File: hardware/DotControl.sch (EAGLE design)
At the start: 26 parts, among them CN1 1X4-BIG, J3 USB-MICROB, SW2 Previous, SW5 Previous, SW6 Next, SW8 Ok, U1 ATMEGA328P-MU-QFN32, U2 TMP102

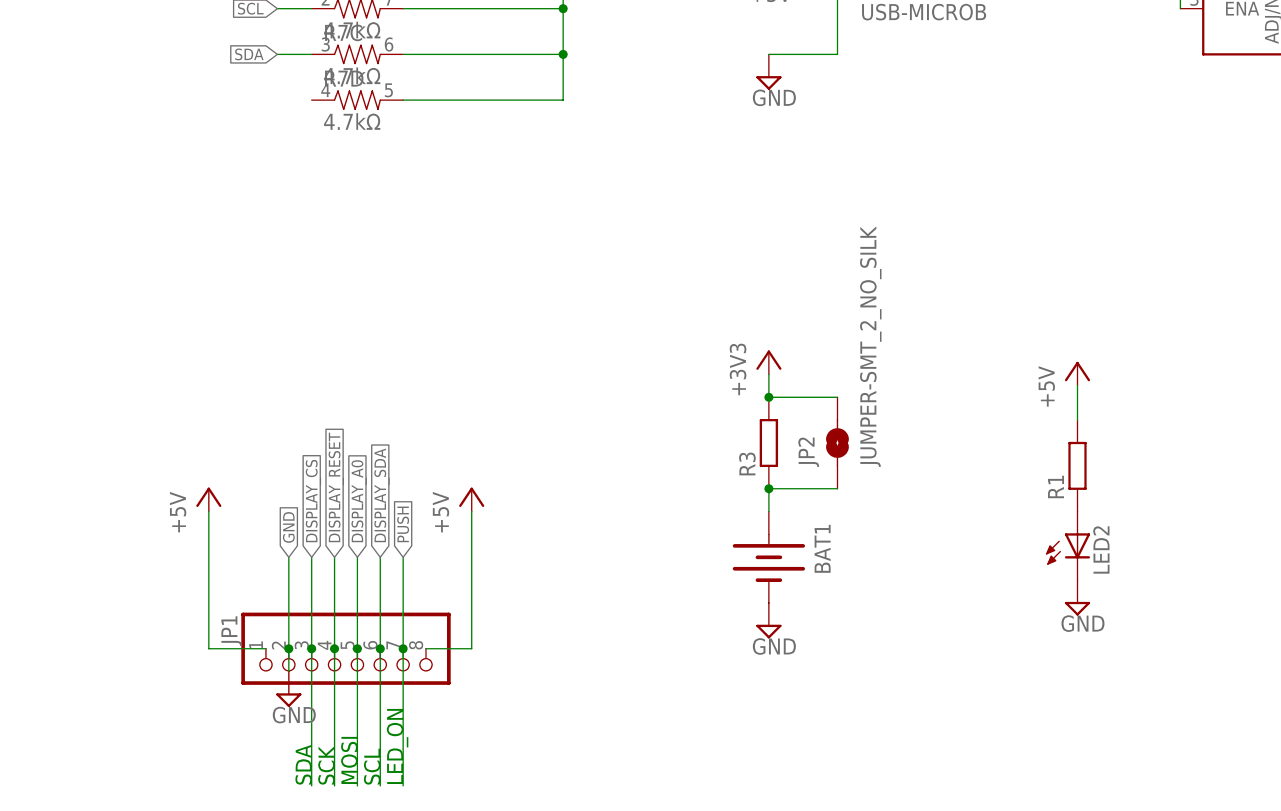
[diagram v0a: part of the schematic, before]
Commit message: Update display supply to 3.3V, charging of battery
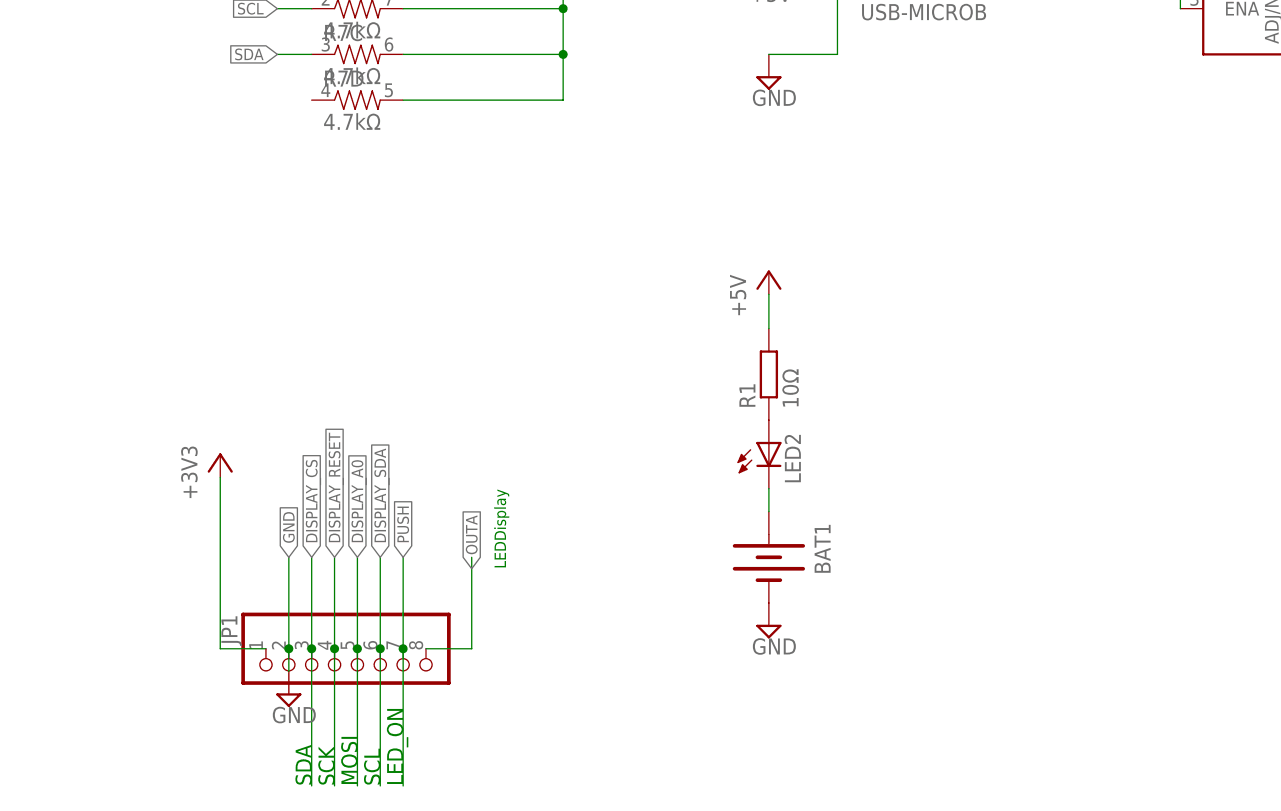
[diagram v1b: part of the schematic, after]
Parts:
- removed JP2: JUMPER-SMT_2_NO_SILK, SparkFun-Jumpers:JUMPER-SMT_2_NO_SILK
- removed R3: (no value), resistor:R-EU_R0603
- R1: value (none) -> 10Ω
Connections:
- removed net N$16: BAT1.+, JP2.1, R3.1
- new net N$3: BAT1.+, LED2.C
- net +3V3: now also JP1.1; no longer JP2.2, R3.2
- net +5V: no longer JP1.1, JP1.8
- net GND: no longer LED2.C
- net OUTA: now also JP1.8
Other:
- note added: "LEDDisplay"
- moved on the sheet: LED2, R1
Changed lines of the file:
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@@
 <setting verticaltext="up"/>
 </settings>
-<grid distance="0.1" unitdist="inch" unit="inch" style="lines" multiple="1" display="no" altdistance="0.01" altunitdist="inch" altunit="inch"/>
+<grid distance="0.05" unitdist="inch" unit="inch" style="lines" multiple="1" display="no" altdistance="0.01" altunitdist="inch" altunit="inch"/>
 <layers>
 <layer number="1" name="Top" color="4" fill="1" visible="no" active="no"/>
@@
 <part name="JP1" library="adafruit" deviceset="PINHD-1X8" device="CLEANBIG"/>
 <part name="SUPPLY8" library="supply2" deviceset="GND" device=""/>
-<part name="+3V3" library="supply1" deviceset="+3V3" device=""/>
 <part name="BAT1" library="Battery" deviceset="BATTERY" device="20PTH"/>
 <part name="+3V14" library="supply1" deviceset="+3V3" device=""/>
@@
 <part name="SUPPLY18" library="supply2" deviceset="GND" device=""/>
 <part name="CN1" library="adafruit" deviceset="1X4" device="-BIG"/>
-<part name="R3" library="resistor" deviceset="R-EU_" device="R0603"/>
-<part name="JP2" library="SparkFun-Jumpers" deviceset="JUMPER-SMT_2_NO" device="_SILK"/>
 <part name="SJ1" library="SparkFun" deviceset="SOLDERJUMPER" device="TRACE"/>
 <part name="+3V7" library="supply1" deviceset="+3V3" device=""/>
-<part name="R1" library="resistor" deviceset="R-EU_" device="R0603"/>
+<part name="R1" library="resistor" deviceset="R-EU_" device="R0603" value="10Ω"/>
 <part name="LED2" library="SparkFun" deviceset="LED" device="0603"/>
-<part name="SUPPLY5" library="supply2" deviceset="GND" device=""/>
-<part name="P+1" library="supply1" deviceset="+5V" device=""/>
-<part name="P+2" library="supply1" deviceset="+5V" device=""/>
 <part name="P+5" library="supply1" deviceset="+5V" device=""/>
 <part name="U2" library="SparkFun" deviceset="TMP102" device=""/>
@@
 <part name="SUPPLY12" library="supply2" deviceset="GND" device=""/>
 <part name="SUPPLY7" library="supply2" deviceset="GND" device=""/>
+<part name="+3V3" library="supply1" deviceset="+3V3" device=""/>
 </parts>
 <sheets>
@@
 <text x="71.12" y="114.3" size="1.778" layer="91" rot="R90">SCL</text>
 <text x="73.66" y="114.3" size="1.778" layer="91" rot="R90">LED_ON</text>
+<text x="85.09" y="138.43" size="1.27" layer="91" rot="R90">LEDDisplay</text>
 </plain>
 <instances>
@@
 <instance part="JP1" gate="G$1" x="66.04" y="127" rot="MR270"/>
 <instance part="SUPPLY8" gate="GND" x="114.3" y="132.08"/>
-<instance part="+3V3" gate="G$1" x="114.3" y="162.56"/>
 <instance part="BAT1" gate="G$1" x="114.3" y="139.7" rot="R270"/>
 <instance part="+3V14" gate="G$1" x="177.8" y="289.56"/>
@@
 <instance part="SUPPLY18" gate="GND" x="218.44" y="157.48"/>
 <instance part="CN1" gate="G$1" x="231.14" y="165.1"/>
-<instance part="R3" gate="G$1" x="114.3" y="152.4" rot="R90"/>
-<instance part="JP2" gate="G$1" x="121.92" y="152.4" rot="R90"/>
 <instance part="SJ1" gate="1" x="80.01" y="219.71" rot="R90"/>
 <instance part="+3V7" gate="G$1" x="80.01" y="227.33"/>
-<instance part="R1" gate="G$1" x="148.59" y="149.86" rot="R90"/>
-<instance part="LED2" gate="G$1" x="148.59" y="142.24"/>
-<instance part="SUPPLY5" gate="GND" x="148.59" y="134.62"/>
-<instance part="P+1" gate="1" x="81.28" y="147.32"/>
-<instance part="P+2" gate="1" x="52.07" y="147.32"/>
-<instance part="P+5" gate="1" x="148.59" y="161.29"/>
+<instance part="R1" gate="G$1" x="114.3" y="160.02" rot="R90"/>
+<instance part="LED2" gate="G$1" x="114.3" y="152.4"/>
+<instance part="P+5" gate="1" x="114.3" y="171.45"/>
 <instance part="U2" gate="G$1" x="226.06" y="104.14"/>
 <instance part="SUPPLY15" gate="GND" x="213.36" y="96.52"/>
@@
 <instance part="SUPPLY12" gate="GND" x="203.2" y="99.06"/>
 <instance part="SUPPLY7" gate="GND" x="254" y="96.52"/>
+<instance part="+3V3" gate="G$1" x="53.34" y="151.13"/>
 </instances>
 <busses>
@@
 <pinref part="SUPPLY19" gate="GND" pin="GND"/>
 <wire x1="62.23" y1="220.98" x2="62.23" y2="227.33" width="0.1524" layer="91"/>
-</segment>
-<segment>
-<pinref part="LED2" gate="G$1" pin="C"/>
-<pinref part="SUPPLY5" gate="GND" pin="GND"/>
 </segment>
 <segment>
@@
 </segment>
 <segment>
-<pinref part="+3V3" gate="G$1" pin="+3V3"/>
-<pinref part="R3" gate="G$1" pin="2"/>
-<wire x1="114.3" y1="157.48" x2="114.3" y2="160.02" width="0.1524" layer="91"/>
-<wire x1="121.92" y1="157.48" x2="114.3" y2="157.48" width="0.1524" layer="91"/>
-<junction x="114.3" y="157.48"/>
-<pinref part="JP2" gate="G$1" pin="2"/>
-</segment>
-<segment>
 <pinref part="SJ1" gate="1" pin="2"/>
 <pinref part="+3V7" gate="G$1" pin="+3V3"/>
@@
 <junction x="203.2" y="109.22"/>
 <pinref part="U2" gate="G$1" pin="VCC"/>
+</segment>
+<segment>
+<pinref part="+3V3" gate="G$1" pin="+3V3"/>
+<pinref part="JP1" gate="G$1" pin="1"/>
+<wire x1="53.34" y1="148.59" x2="53.34" y2="129.54" width="0.1524" layer="91"/>
+<wire x1="53.34" y1="129.54" x2="58.42" y2="129.54" width="0.1524" layer="91"/>
 </segment>
 </net>
@@
 </segment>
 <segment>
-<pinref part="P+1" gate="1" pin="+5V"/>
-<wire x1="81.28" y1="144.78" x2="81.28" y2="129.54" width="0.1524" layer="91"/>
-<pinref part="JP1" gate="G$1" pin="8"/>
-<wire x1="76.2" y1="129.54" x2="81.28" y2="129.54" width="0.1524" layer="91"/>
-</segment>
-<segment>
-<pinref part="P+2" gate="1" pin="+5V"/>
-<pinref part="JP1" gate="G$1" pin="1"/>
-<wire x1="52.07" y1="144.78" x2="52.07" y2="129.54" width="0.1524" layer="91"/>
-<wire x1="52.07" y1="129.54" x2="58.42" y2="129.54" width="0.1524" layer="91"/>
-</segment>
-<segment>
 <pinref part="R1" gate="G$1" pin="2"/>
-<wire x1="148.59" y1="154.94" x2="148.59" y2="158.75" width="0.1524" layer="91"/>
+<wire x1="114.3" y1="165.1" x2="114.3" y2="168.91" width="0.1524" layer="91"/>
 <pinref part="P+5" gate="1" pin="+5V"/>
 </segment>
@@
 <wire x1="327.66" y1="236.22" x2="330.2" y2="236.22" width="0.1524" layer="91"/>
 <label x="330.2" y="236.22" size="1.27" layer="95" xref="yes"/>
+</segment>
+<segment>
+<pinref part="JP1" gate="G$1" pin="8"/>
+<wire x1="76.2" y1="129.54" x2="81.28" y2="129.54" width="0.1524" layer="91"/>
+<wire x1="81.28" y1="129.54" x2="81.28" y2="139.7" width="0.1524" layer="91"/>
+<label x="81.28" y="138.43" size="1.27" layer="95" rot="R90" xref="yes"/>
 </segment>
 </net>
@@
 </segment>
 </net>
-<net name="N$16" class="0">
-<segment>
-<pinref part="R3" gate="G$1" pin="1"/>
-<pinref part="BAT1" gate="G$1" pin="+"/>
-<wire x1="114.3" y1="147.32" x2="114.3" y2="144.78" width="0.1524" layer="91"/>
-<wire x1="121.92" y1="147.32" x2="114.3" y2="147.32" width="0.1524" layer="91"/>
-<junction x="114.3" y="147.32"/>
-<pinref part="JP2" gate="G$1" pin="1"/>
-</segment>
-</net>
 <net name="N$2" class="0">
 <segment>
@@
 </segment>
 </net>
+<net name="N$3" class="0">
+<segment>
+<pinref part="LED2" gate="G$1" pin="C"/>
+<pinref part="BAT1" gate="G$1" pin="+"/>
+<wire x1="114.3" y1="147.32" x2="114.3" y2="144.78" width="0.1524" layer="91"/>
+</segment>
+</net>

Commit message: Amend
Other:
- note removed: "Do not put 3V3 when battery on!"
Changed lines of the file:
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@@
 <setting verticaltext="up"/>
 </settings>
-<grid distance="0.05" unitdist="inch" unit="inch" style="lines" multiple="1" display="no" altdistance="0.01" altunitdist="inch" altunit="inch"/>
+<grid distance="0.1" unitdist="inch" unit="inch" style="lines" multiple="1" display="no" altdistance="0.01" altunitdist="inch" altunit="inch"/>
 <layers>
 <layer number="1" name="Top" color="4" fill="1" visible="no" active="no"/>
@@
 <text x="180.34" y="259.08" size="1.27" layer="91" rot="R90">Green</text>
 <text x="189.738" y="259.08" size="1.27" layer="91">Red</text>
-<text x="223.52" y="177.8" size="1.778" layer="91">Do not put 3V3 when battery on!</text>
 <text x="81.28" y="96.52" size="1.27" layer="91">Always enable internal pullup beforehand!</text>
 <text x="238.76" y="91.44" size="1.778" layer="91">Temperature

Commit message: Add CryptoAuthentication module
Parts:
- added U3: ATSHA204-TSU, SparkFun-IC-Special-Function:ATSHA204-TSU
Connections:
- net +3V3: now also U3.VCC
- net ADCENA: now also U3.SDA
- net GND: now also U3.GND
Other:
- note added: "Authentification module"
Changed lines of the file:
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@@
 <part name="SUPPLY7" library="supply2" deviceset="GND" device=""/>
 <part name="+3V3" library="supply1" deviceset="+3V3" device=""/>
+<part name="U3" library="SparkFun-IC-Special-Function" deviceset="ATSHA204" device="-TSU"/>
+<part name="+3V10" library="supply1" deviceset="+3V3" device=""/>
+<part name="SUPPLY5" library="supply2" deviceset="GND" device=""/>
 </parts>
 <sheets>
@@
 <text x="73.66" y="114.3" size="1.778" layer="91" rot="R90">LED_ON</text>
 <text x="85.09" y="138.43" size="1.27" layer="91" rot="R90">LEDDisplay</text>
+<text x="208.28" y="71.12" size="3.81" layer="91">Authentification module</text>
 </plain>
 <instances>
@@
 <instance part="SUPPLY7" gate="GND" x="254" y="96.52"/>
 <instance part="+3V3" gate="G$1" x="53.34" y="151.13"/>
+<instance part="U3" gate="G$1" x="215.9" y="58.42"/>
+<instance part="+3V10" gate="G$1" x="228.6" y="63.5"/>
+<instance part="SUPPLY5" gate="GND" x="228.6" y="53.34"/>
 </instances>
 <busses>
@@
 <wire x1="236.22" y1="99.06" x2="254" y2="99.06" width="0.1524" layer="91"/>
 <pinref part="SUPPLY7" gate="GND" pin="GND"/>
+</segment>
+<segment>
+<pinref part="U3" gate="G$1" pin="GND"/>
+<wire x1="223.52" y1="55.88" x2="228.6" y2="55.88" width="0.1524" layer="91"/>
+<pinref part="SUPPLY5" gate="GND" pin="GND"/>
 </segment>
 </net>
@@
 <wire x1="53.34" y1="129.54" x2="58.42" y2="129.54" width="0.1524" layer="91"/>
 </segment>
+<segment>
+<pinref part="U3" gate="G$1" pin="VCC"/>
+<wire x1="223.52" y1="60.96" x2="228.6" y2="60.96" width="0.1524" layer="91"/>
+<pinref part="+3V10" gate="G$1" pin="+3V3"/>
+</segment>
 </net>
 <net name="PUSH" class="0">
@@
 <wire x1="83.82" y1="83.82" x2="83.82" y2="60.96" width="0.1524" layer="91"/>
 </segment>
-</net>
+<segment>
+<pinref part="U3" gate="G$1" pin="SDA"/>
+<wire x1="205.74" y1="58.42" x2="200.66" y2="58.42" width="0.1524" layer="91"/>
+<label x="200.66" y="58.42" size="1.27" layer="95" rot="R180" xref="yes"/>
+</segment>
+</net>

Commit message: Add PCB antenna
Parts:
- added SJ2: SOLDERJUMPERTRACE, SparkFun:SOLDERJUMPERTRACE
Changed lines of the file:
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@@
 <part name="+3V10" library="supply1" deviceset="+3V3" device=""/>
 <part name="SUPPLY5" library="supply2" deviceset="GND" device=""/>
+<part name="SJ2" library="SparkFun" deviceset="SOLDERJUMPER" device="TRACE"/>
 </parts>
 <sheets>
@@
 <instance part="+3V10" gate="G$1" x="228.6" y="63.5"/>
 <instance part="SUPPLY5" gate="GND" x="228.6" y="53.34"/>
+<instance part="SJ2" gate="1" x="217.17" y="34.29" rot="R180"/>
 </instances>
 <busses>

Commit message: Add missing 3V3 connection to battery
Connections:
- removed net N$3: BAT1.+, LED2.C
- net +3V3: now also BAT1.+, LED2.C
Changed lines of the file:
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@@
 <part name="SUPPLY5" library="supply2" deviceset="GND" device=""/>
 <part name="SJ2" library="SparkFun" deviceset="SOLDERJUMPER" device="TRACE"/>
+<part name="+3V9" library="supply1" deviceset="+3V3" device=""/>
 </parts>
 <sheets>
@@
 <instance part="SUPPLY5" gate="GND" x="228.6" y="53.34"/>
 <instance part="SJ2" gate="1" x="217.17" y="34.29" rot="R180"/>
+<instance part="+3V9" gate="G$1" x="134.62" y="149.86"/>
 </instances>
 <busses>
@@
 <pinref part="+3V10" gate="G$1" pin="+3V3"/>
 </segment>
+<segment>
+<pinref part="LED2" gate="G$1" pin="C"/>
+<pinref part="BAT1" gate="G$1" pin="+"/>
+<wire x1="114.3" y1="147.32" x2="114.3" y2="144.78" width="0.1524" layer="91"/>
+<pinref part="+3V9" gate="G$1" pin="+3V3"/>
+<wire x1="134.62" y1="147.32" x2="114.3" y2="147.32" width="0.1524" layer="91"/>
+<junction x="114.3" y="147.32"/>
+</segment>
 </net>
 <net name="PUSH" class="0">
@@
 </segment>
 </net>
-<net name="N$3" class="0">
-<segment>
-<pinref part="LED2" gate="G$1" pin="C"/>
-<pinref part="BAT1" gate="G$1" pin="+"/>
-<wire x1="114.3" y1="147.32" x2="114.3" y2="144.78" width="0.1524" layer="91"/>
-</segment>
-</net>
